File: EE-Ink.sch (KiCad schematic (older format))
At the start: 13 parts, among them U1 ED060SC4, U2 STM32F030C

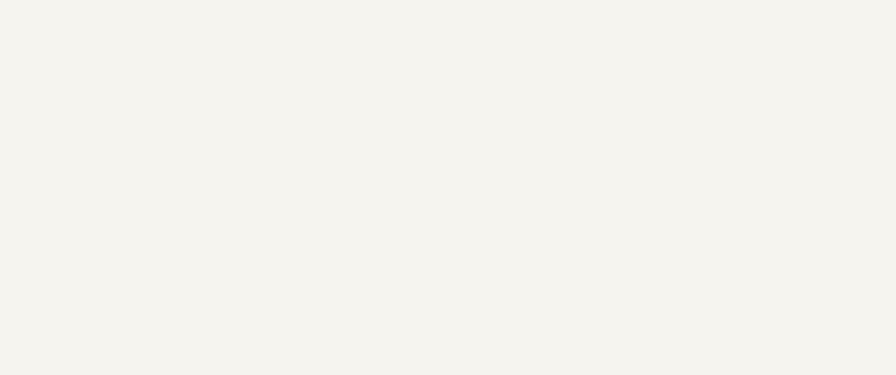
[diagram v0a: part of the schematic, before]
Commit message: Fixing transistor connections and adding UART stuff.
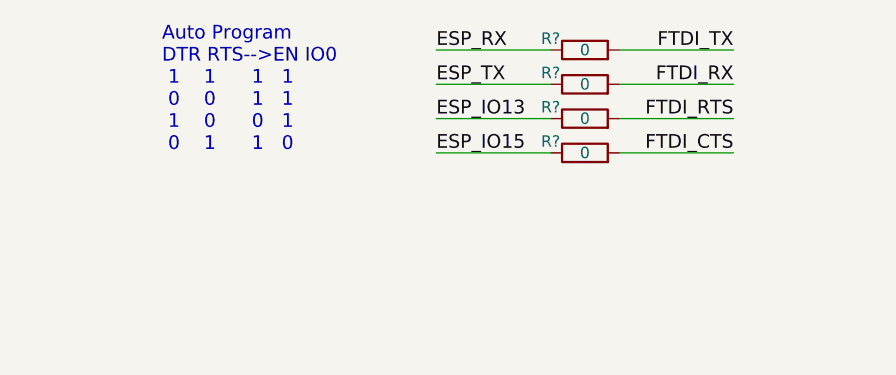
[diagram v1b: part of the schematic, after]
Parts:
- added R? (x4): 0, symbol R
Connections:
- net labels added: ESP_IO13, ESP_IO15, ESP_RX, ESP_TX
- wire segments 116 -> 124
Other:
- note added: "Auto Program\nDTR RTS-->EN IO0\n 1 1 1 1\n 0 0 1 1\n 1 0 0 1\n 0 1 1 0"
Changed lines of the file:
@@
 NoConn ~ 10300 5300
 NoConn ~ 10300 5200
+$Comp
+L R R?
+U 1 1 58E07741
+P 6350 1050
+F 0 "R?" V 6400 1200 50  0000 C CNN
+F 1 "0" V 6350 1050 50  0000 C CNN
+F 2 "" V 6280 1050 50  0001 C CNN
+F 3 "" H 6350 1050 50  0001 C CNN
+	1    6350 1050
+	0    -1   -1   0
+$EndComp
+$Comp
+L R R?
+U 1 1 58E07958
+P 6350 1200
+F 0 "R?" V 6400 1350 50  0000 C CNN
+F 1 "0" V 6350 1200 50  0000 C CNN
+F 2 "" V 6280 1200 50  0001 C CNN
+F 3 "" H 6350 1200 50  0001 C CNN
+	1    6350 1200
+	0    -1   -1   0
+$EndComp
+$Comp
+L R R?
+U 1 1 58E07A7F
+P 6350 1350
+F 0 "R?" V 6400 1500 50  0000 C CNN
+F 1 "0" V 6350 1350 50  0000 C CNN
+F 2 "" V 6280 1350 50  0001 C CNN
+F 3 "" H 6350 1350 50  0001 C CNN
+	1    6350 1350
+	0    -1   -1   0
+$EndComp
+$Comp
+L R R?
+U 1 1 58E07AC1
+P 6350 1500
+F 0 "R?" V 6400 1650 50  0000 C CNN
+F 1 "0" V 6350 1500 50  0000 C CNN
+F 2 "" V 6280 1500 50  0001 C CNN
+F 3 "" H 6350 1500 50  0001 C CNN
+	1    6350 1500
+	0    -1   -1   0
+$EndComp
+Text Label 7000 1200 2    60   ~ 0
+FTDI_RX
+Text Label 7000 1050 2    60   ~ 0
+FTDI_TX
+Wire Wire Line
+	6500 1050 7000 1050
+Wire Wire Line
+	6500 1200 7000 1200
+Wire Wire Line
+	6500 1350 7000 1350
+Wire Wire Line
+	6500 1500 7000 1500
+Text Label 7000 1350 2    60   ~ 0
+FTDI_RTS
+Text Label 7000 1500 2    60   ~ 0
+FTDI_CTS
+Wire Wire Line
+	6200 1500 5700 1500
+Text Label 5700 1500 0    60   ~ 0
+ESP_IO15
+Wire Wire Line
+	6200 1050 5700 1050
+Wire Wire Line
+	6200 1200 5700 1200
+Wire Wire Line
+	6200 1350 5700 1350
+Text Label 5700 1350 0    60   ~ 0
+ESP_IO13
+Text Label 5700 1200 0    60   ~ 0
+ESP_TX
+Text Label 5700 1050 0    60   ~ 0
+ESP_RX
+Text Notes 4500 1500 0    60   ~ 0
+   Auto Program\nDTR RTS-->EN IO0\n 1    1      1   1\n 0    0      1   1\n 1    0      0   1\n 0    1      1   0
 $EndSCHEMATC

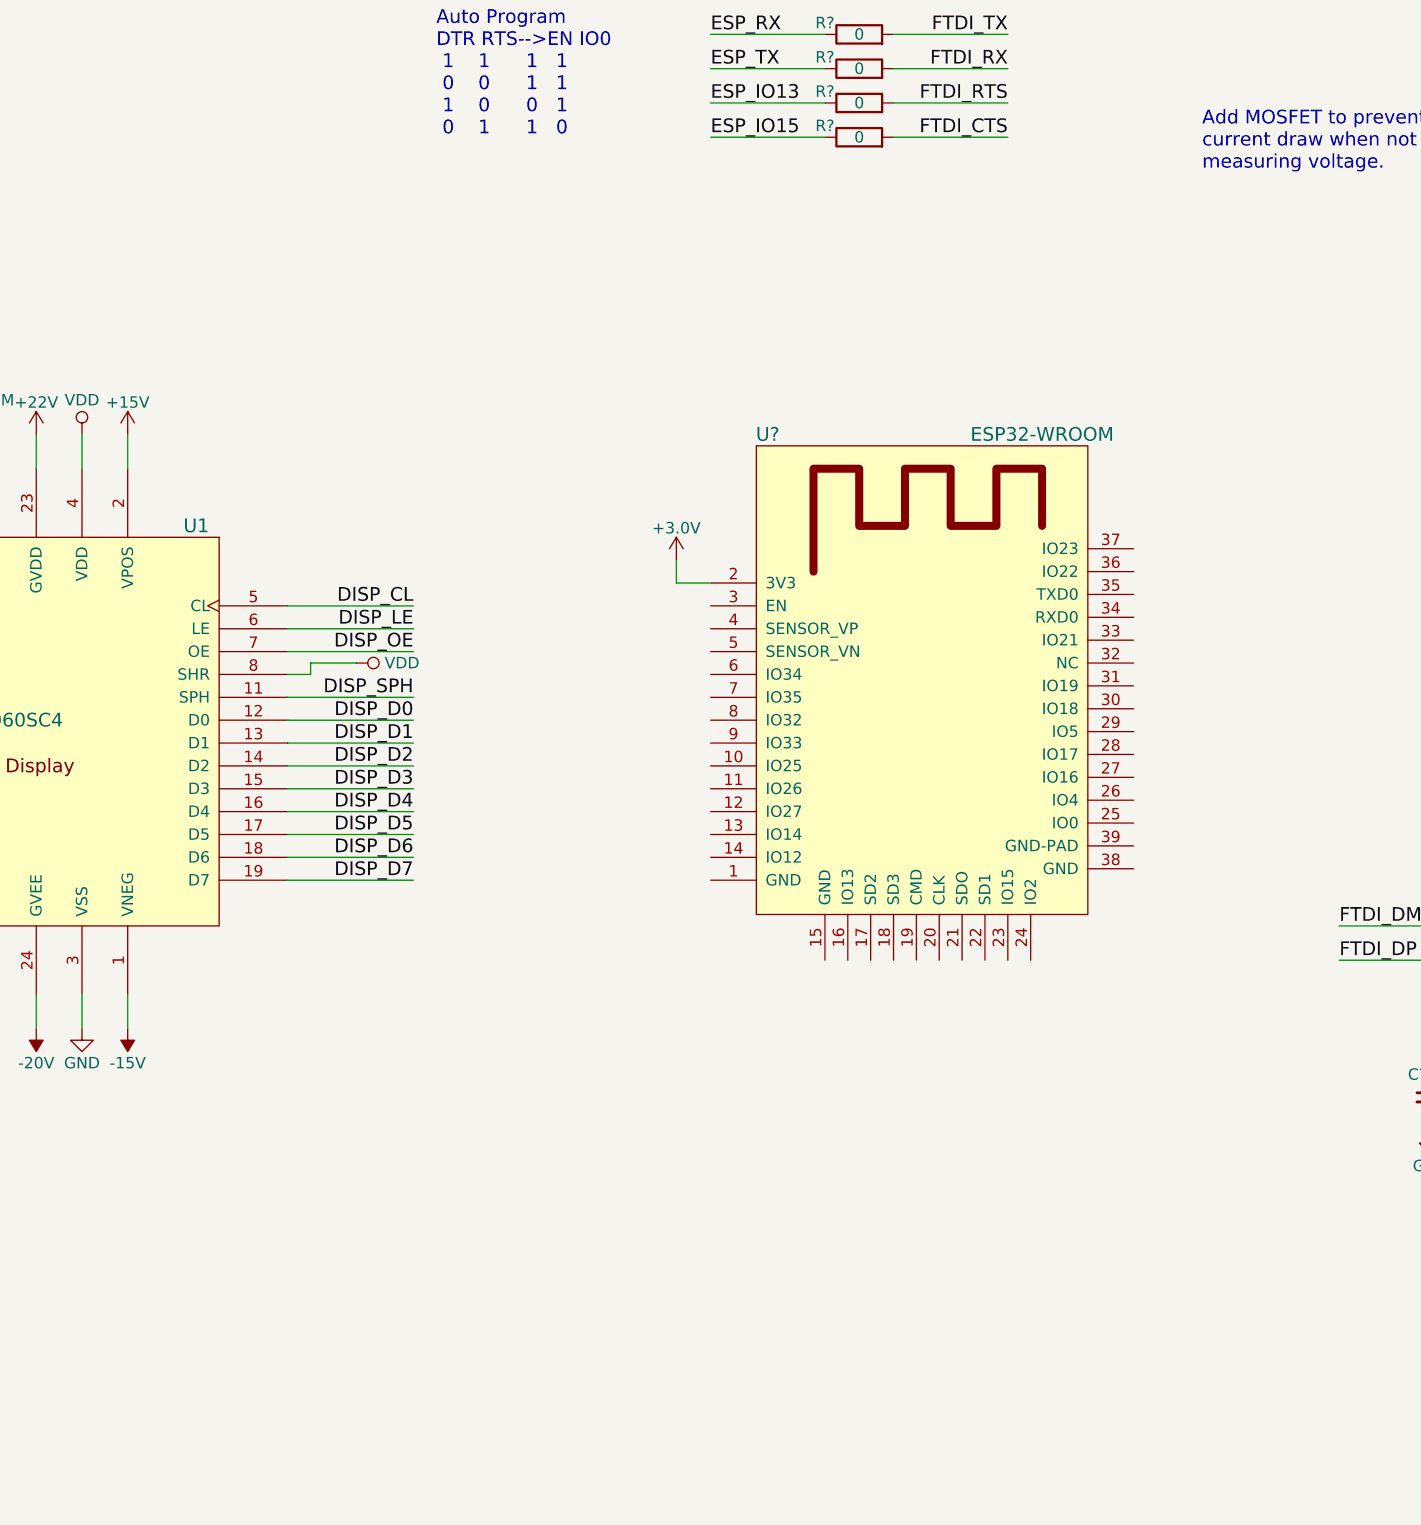
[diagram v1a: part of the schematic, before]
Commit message: Began wiring up ESP32's IO pins.
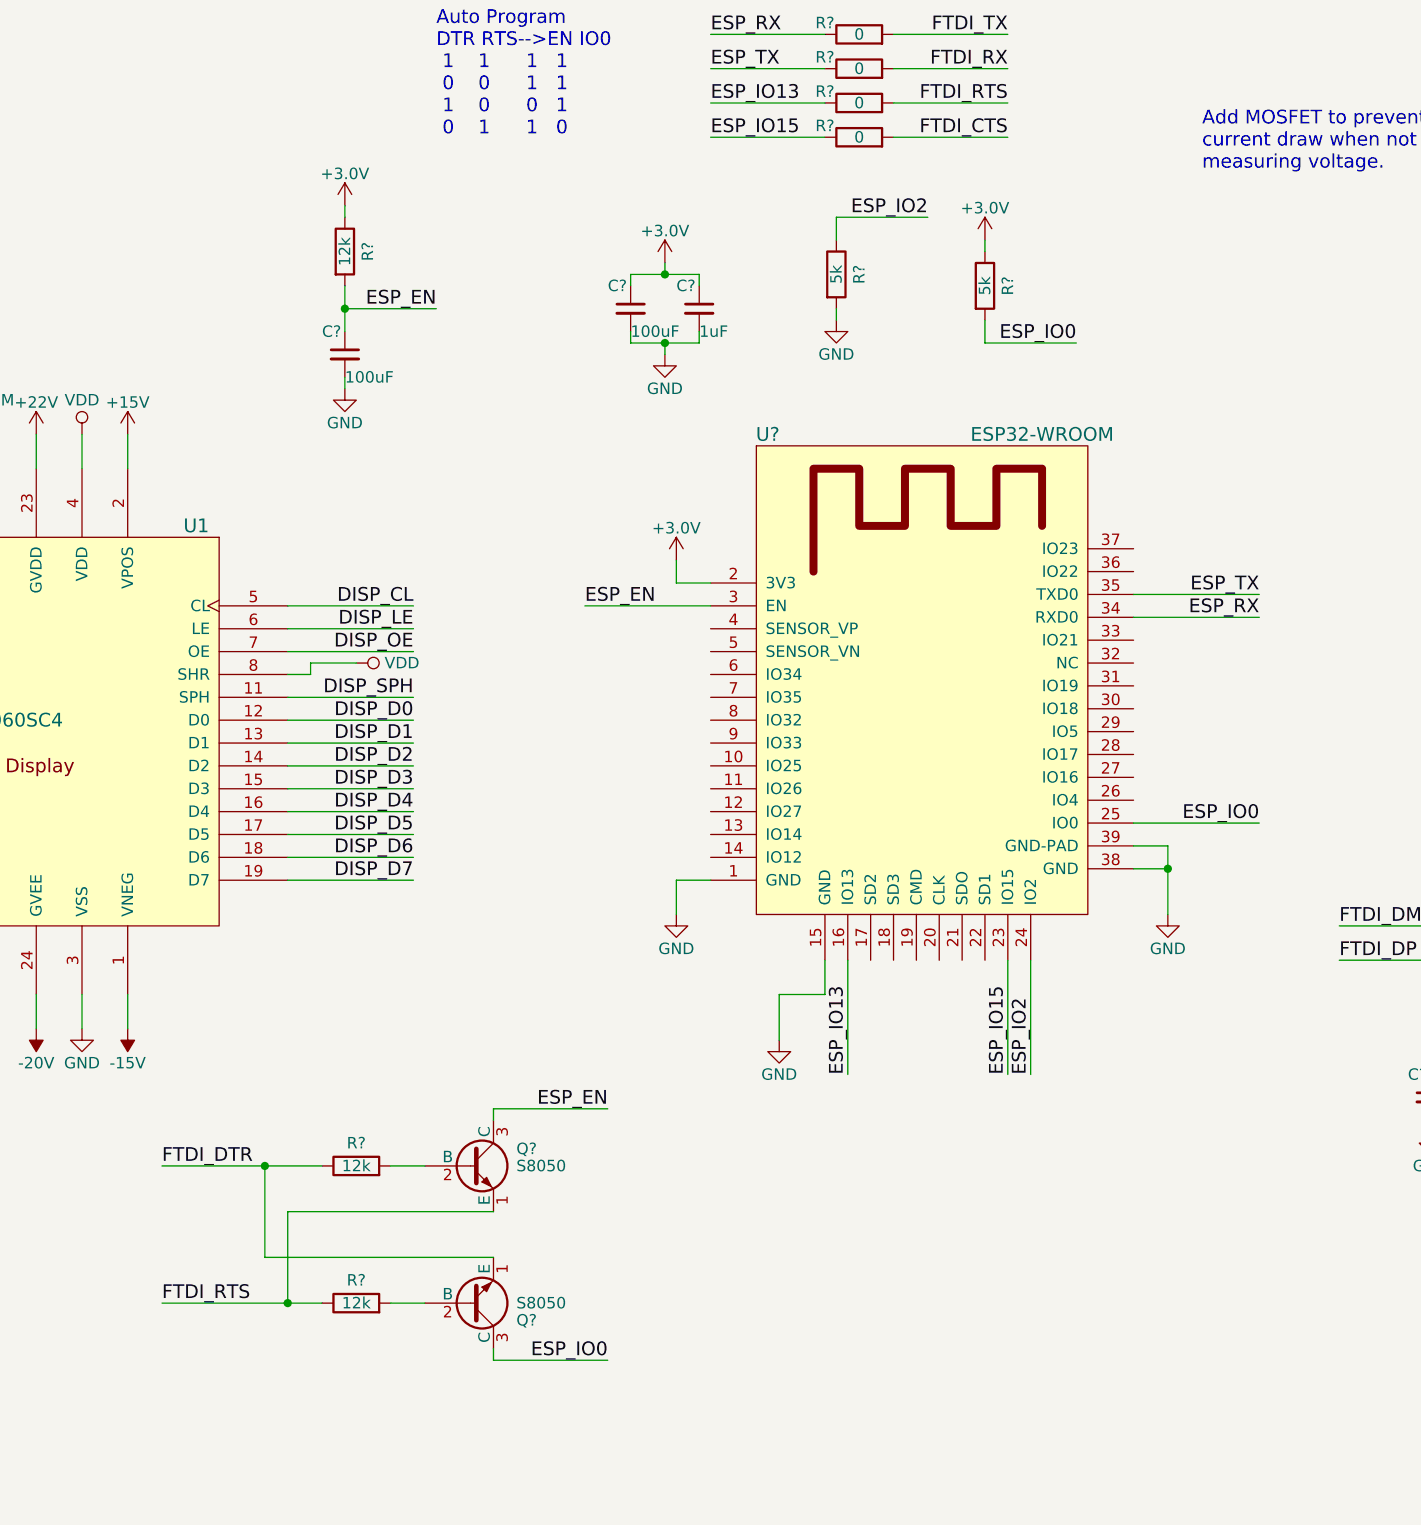
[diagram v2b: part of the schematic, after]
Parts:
- added C? (x2): 100uF, symbol C_Small
- added C?: 1uF, symbol C_Small
- added Q? (x2): S8050, TO_SOT_Packages_THT:TO-92_Molded_Narrow, symbol S8050
- added R? (x3): 12k, symbol R
- added R? (x2): 5k, symbol R
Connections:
- net labels added: ESP_EN, ESP_IO0, ESP_IO2
- wire segments 124 -> 169

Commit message: Finished wiring up ESP32 pins.
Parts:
- removed D1: LED_Small, symbol LED_Small
- removed R1: 10k, symbol R
- removed R2: 15k, symbol R
- removed R3: 470, symbol R
- removed R?: 5k, symbol R
- removed U2: STM32F030C, symbol STM32F030C
- added R? (x2): 0, symbol R
- added R?: 5k, symbol R
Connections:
- net labels removed: +BATT, BATT_V, LED_STATUS, PROG_SWCLK, PROG_SWDIO, SPI1_MISO, SPI1_MOSI, SPI1_NSS, SPI1_SCK, USART1_RX, USART1_TX
- wire segments 169 -> 152
- no-connect marks 8 -> 13
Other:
- note removed: "Add MOSFET to prevent\ncurrent draw when not\nmeasuring voltage."
- note removed: "Is it OK to drive this LED directly?"
- moved on the sheet: C?, Q?, R?
